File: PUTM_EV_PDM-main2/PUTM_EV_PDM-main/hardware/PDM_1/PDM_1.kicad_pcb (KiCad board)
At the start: 4 copper layers, 60 x 90 mm, 115 parts, among them IC2 BTS722204ESAXUMA1, IC3 BTS722204ESAXUMA1, IC4 BTS722204ESAXUMA1, IC5 BTS722204ESAXUMA1, U1 STM32G0C1KCTxN, U2 LD1117S33TR_SOT223, U3 LM2675M-5, U5 MCP2542FDxMF

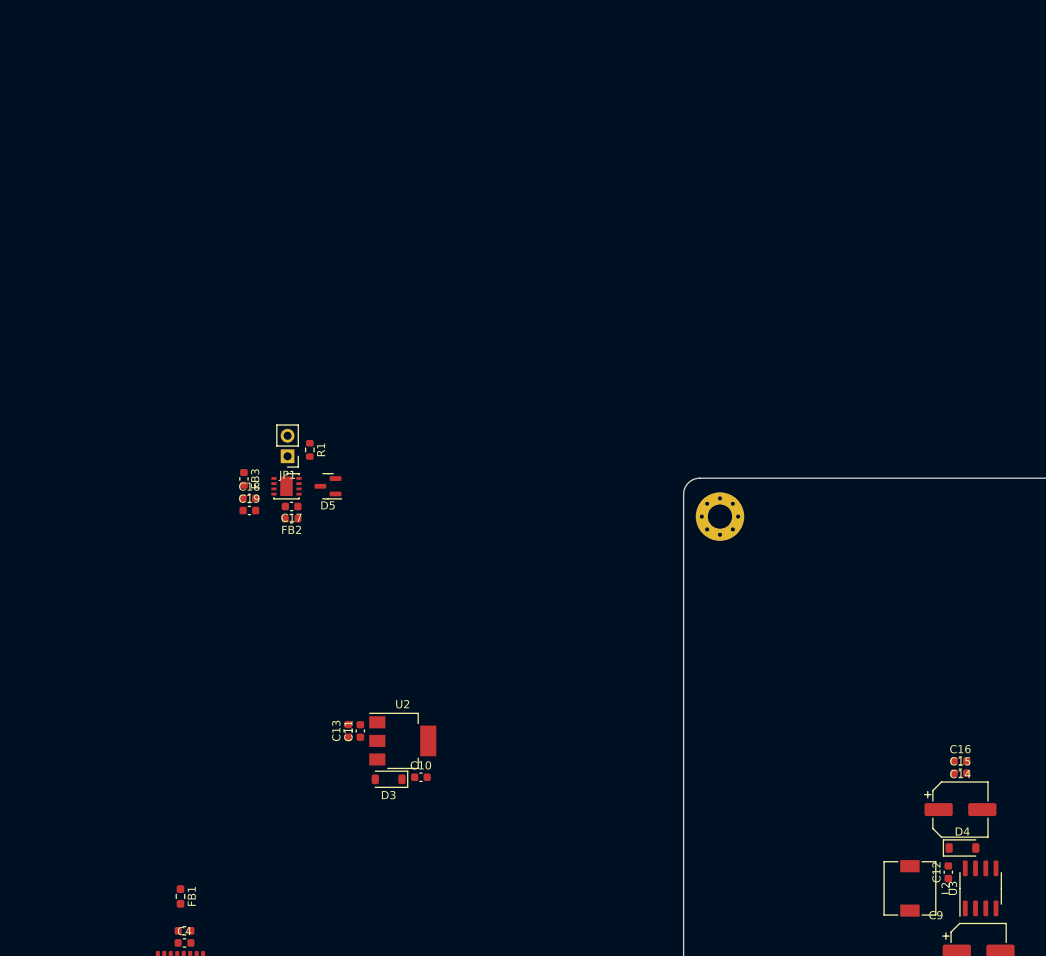
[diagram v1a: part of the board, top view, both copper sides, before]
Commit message: małe zmiany
dodano złącza
zmieniono parę footprintów
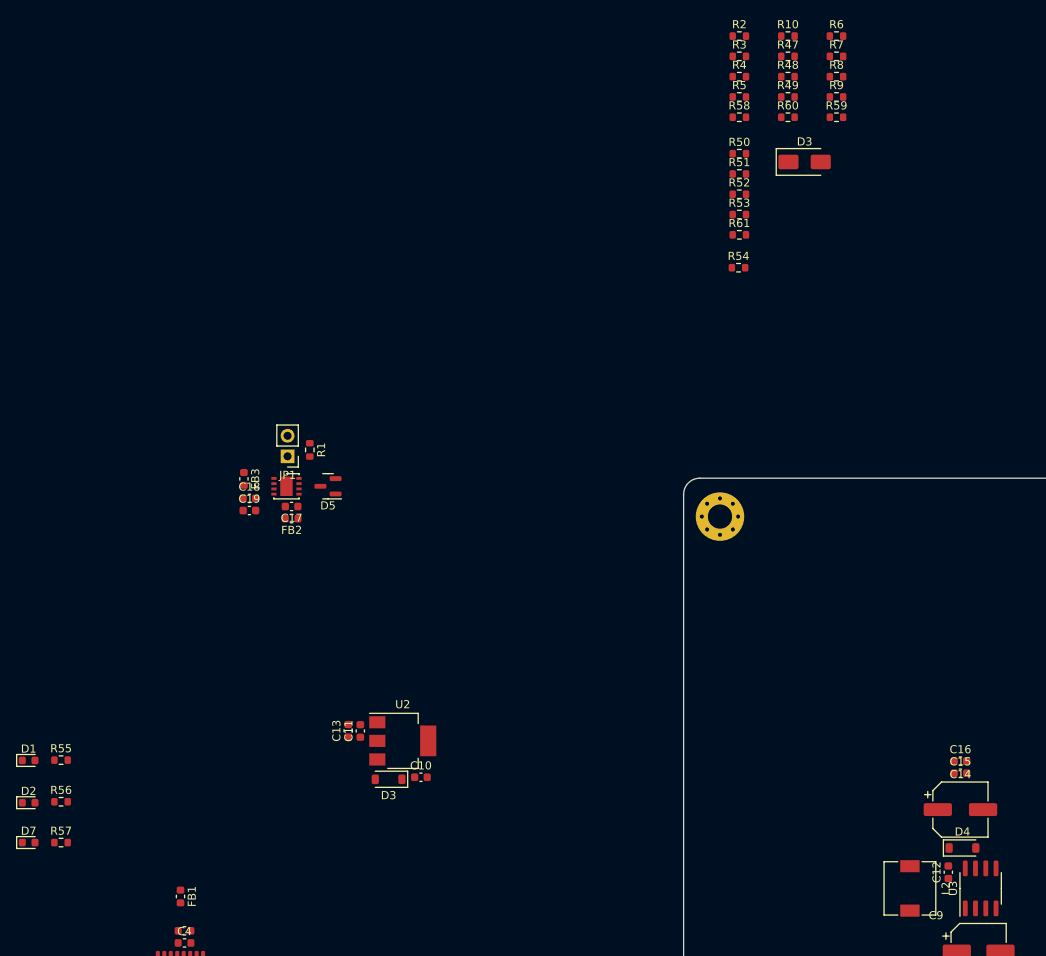
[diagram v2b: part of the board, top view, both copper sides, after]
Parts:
- added D1: LED, LED_SMD:LED_0603_1608Metric, F.Cu at (35.0, 110.9)
- added D2: LED, LED_SMD:LED_0603_1608Metric, F.Cu at (35.0, 116.2)
- added D3: PESD24VF1BLYL, Diode_SMD:D_SMA, F.Cu at (131.0, 36.9)
- added D7: LED, LED_SMD:LED_0603_1608Metric, F.Cu at (35.0, 121.1)
- added R10: 1.2k, Resistor_SMD:R_0603_1608Metric, F.Cu at (128.9, 21.3)
- added R2: 1.2k, Resistor_SMD:R_0603_1608Metric, F.Cu at (122.9, 21.3)
- added R3: 1.2k, Resistor_SMD:R_0603_1608Metric, F.Cu at (122.9, 23.8)
- added R4: 1.2k, Resistor_SMD:R_0603_1608Metric, F.Cu at (122.9, 26.3)
- added R47: 1.2k, Resistor_SMD:R_0603_1608Metric, F.Cu at (128.9, 23.8)
- added R48: 1.2k, Resistor_SMD:R_0603_1608Metric, F.Cu at (128.9, 26.3)
- added R49: 1.2k, Resistor_SMD:R_0603_1608Metric, F.Cu at (128.9, 28.8)
- added R5: 1.2k, Resistor_SMD:R_0603_1608Metric, F.Cu at (122.9, 28.8)
- added R50: 1.2k, Resistor_SMD:R_0603_1608Metric, F.Cu at (122.9, 35.9)
- added R51: 1.2k, Resistor_SMD:R_0603_1608Metric, F.Cu at (122.9, 38.4)
- added R52: 1.2k, Resistor_SMD:R_0603_1608Metric, F.Cu at (122.9, 40.9)
- added R53: 1.2k, Resistor_SMD:R_0603_1608Metric, F.Cu at (122.9, 43.4)
- added R54: 100k, Resistor_SMD:R_0603_1608Metric, F.Cu at (122.8, 50.0)
- added R55: 330, Resistor_SMD:R_0603_1608Metric, F.Cu at (39.0, 110.9)
- added R56: 330, Resistor_SMD:R_0603_1608Metric, F.Cu at (39.0, 116.0)
- added R57: 330, Resistor_SMD:R_0603_1608Metric, F.Cu at (39.0, 121.1)
- added R58: 4.7k, Resistor_SMD:R_0603_1608Metric, F.Cu at (122.9, 31.3)
- added R59: 4.7k, Resistor_SMD:R_0603_1608Metric, F.Cu at (134.9, 31.3)
- added R6: 1.2k, Resistor_SMD:R_0603_1608Metric, F.Cu at (134.9, 21.3)
- added R60: 4.7k, Resistor_SMD:R_0603_1608Metric, F.Cu at (128.9, 31.3)
- added R61: 4.7k, Resistor_SMD:R_0603_1608Metric, F.Cu at (122.9, 45.9)
- added R7: 1.2k, Resistor_SMD:R_0603_1608Metric, F.Cu at (134.9, 23.8)
- added R8: 1.2k, Resistor_SMD:R_0603_1608Metric, F.Cu at (134.9, 26.3)
- added R9: 1.2k, Resistor_SMD:R_0603_1608Metric, F.Cu at (134.9, 28.8)
- C14: footprint Capacitor_SMD:CP_Elec_6.3x7.7 -> Capacitor_SMD:CP_Elec_6.3x5.4
- FB1: footprint Resistor_SMD:R_0603_1608Metric_Pad0.98x0.95mm_HandSolder -> Inductor_SMD:L_0603_1608Metric
- R14, R15, R16, R17, R23, R24, R25, R26, R32, R33, R34, R35, R41, R42, R43, R44: value 4.7k -> 10k
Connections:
- net +24V renamed Net-(Dr1-A)
- net /battery connection/IC_1/out0 renamed OUT1_0
- net /battery connection/IC_1/out1 renamed OUT1_1
- net /battery connection/IC_1/out2 renamed OUT1_2
- net /battery connection/IC_1/out3 renamed OUT1_3
- net /battery connection/IC_2/out0 renamed OUT2_0
- net /battery connection/IC_2/out1 renamed OUT2_1
- net /battery connection/IC_2/out2 renamed OUT2_2
- net /battery connection/IC_2/out3 renamed OUT2_3
- net /battery connection/IC_3/out0 renamed OUT3_0
- net /battery connection/IC_3/out1 renamed OUT3_1
- net /battery connection/IC_3/out2 renamed OUT3_2
- net /battery connection/IC_3/out3 renamed OUT3_3
- net /battery connection/IC_4/out0 renamed OUT4_0
- net /battery connection/IC_4/out1 renamed OUT4_1
- net /battery connection/IC_4/out2 renamed OUT4_2
- net /battery connection/IC_4/out3 renamed OUT4_3
- C10 pad 1: Net-(D3-K) -> +5V
- C29 pad 1: /battery connection/IC_1/ADC -> /FUSE1_IS
- C30 pad 1: Net-(C30-Pad1) -> +BATT
- C31 pad 1: Net-(C30-Pad1) -> +BATT
- C31 pad 2: Net-(C31-Pad2) -> Net-(IC2-GND_1)
- C32 pad 1: Net-(C31-Pad2) -> Net-(IC2-GND_1)
- C37 pad 1: /battery connection/IC_2/ADC -> /FUSE2_IS
- C38 pad 1: Net-(C38-Pad1) -> +BATT
- C39 pad 1: Net-(C38-Pad1) -> +BATT
- C39 pad 2: Net-(C39-Pad2) -> Net-(IC3-GND_1)
- C40 pad 1: Net-(C39-Pad2) -> Net-(IC3-GND_1)
- C45 pad 1: /battery connection/IC_3/ADC -> /FUSE3_IS
- C46 pad 1: Net-(C46-Pad1) -> +BATT
- C47 pad 1: Net-(C46-Pad1) -> +BATT
- C47 pad 2: Net-(C47-Pad2) -> Net-(IC4-GND_1)
- C48 pad 1: Net-(C47-Pad2) -> Net-(IC4-GND_1)
- C53 pad 1: /battery connection/IC_4/ADC -> /FUSE4_IS
- C54 pad 1: Net-(C54-Pad1) -> +BATT
- C55 pad 1: Net-(C54-Pad1) -> +BATT
- C55 pad 2: Net-(C55-Pad2) -> Net-(IC5-GND_1)
- C56 pad 1: Net-(C55-Pad2) -> Net-(IC5-GND_1)
- IC2 pad 1: unconnected-(IC2-GND_1-Pad1) -> Net-(IC2-GND_1)
- IC2 pad 11: /battery connection/IC_1/4.7k resistor -> /battery connection/IC_1/IN3
- IC2 pad 3: /battery connection/IC_1/1.2k resistor -> Net-(IC2-SO)
- IC2 pad 4: /battery connection/IC_1/1.2k resistor -> Net-(IC2-SI)
- IC2 pad 5: /battery connection/IC_1/1.2k resistor -> Net-(IC2-SCLK)
- IC2 pad 6: /battery connection/IC_1/1.2k resistor -> Net-(IC2-CSN)
- IC2 pad 7: unconnected-(IC2-LHI-Pad7) -> Net-(IC2-LHI)
- IC3 pad 1: unconnected-(IC3-GND_1-Pad1) -> Net-(IC3-GND_1)
- IC3 pad 11: /battery connection/IC_2/4.7k resistor -> /battery connection/IC_2/IN3
- IC3 pad 3: /battery connection/IC_1/1.2k resistor -> Net-(IC3-SO)
- IC3 pad 4: /battery connection/IC_1/1.2k resistor -> Net-(IC3-SI)
- IC3 pad 5: /battery connection/IC_1/1.2k resistor -> Net-(IC3-SCLK)
- IC3 pad 6: /battery connection/IC_1/1.2k resistor -> Net-(IC3-CSN)
- IC3 pad 7: unconnected-(IC3-LHI-Pad7) -> Net-(IC3-LHI)
- IC4 pad 1: unconnected-(IC4-GND_1-Pad1) -> Net-(IC4-GND_1)
- IC4 pad 11: /battery connection/IC_3/4.7k resistor -> /battery connection/IC_3/IN3
- IC4 pad 3: /battery connection/IC_1/1.2k resistor -> Net-(IC4-SO)
- IC4 pad 4: /battery connection/IC_1/1.2k resistor -> Net-(IC4-SI)
- IC4 pad 5: /battery connection/IC_1/1.2k resistor -> Net-(IC4-SCLK)
- IC4 pad 6: /battery connection/IC_1/1.2k resistor -> Net-(IC4-CSN)
- IC4 pad 7: unconnected-(IC4-LHI-Pad7) -> Net-(IC4-LHI)
- IC5 pad 1: unconnected-(IC5-GND_1-Pad1) -> Net-(IC5-GND_1)
- IC5 pad 11: /battery connection/IC_4/4.7k resistor -> /battery connection/IC_4/IN3
- IC5 pad 3: /battery connection/IC_1/1.2k resistor -> Net-(IC5-SO)
- IC5 pad 4: /battery connection/IC_1/1.2k resistor -> Net-(IC5-SI)
- IC5 pad 5: /battery connection/IC_1/1.2k resistor -> Net-(IC5-SCLK)
- IC5 pad 6: /battery connection/IC_1/1.2k resistor -> Net-(IC5-CSN)
- IC5 pad 7: unconnected-(IC5-LHI-Pad7) -> Net-(IC5-LHI)
- R11 pad 1: /battery connection/IC_1/ADC -> /FUSE1_IS
- R14 pad 1: /battery connection/IC_1/IN0 -> GND
- R15 pad 1: /battery connection/IC_1/IN1 -> GND
- R16 pad 1: /battery connection/IC_1/IN2 -> GND
- R17 pad 1: /battery connection/IC_1/IN3 -> GND
- R17 pad 2: /battery connection/IC_1/4.7k resistor -> /battery connection/IC_1/IN3
- R18 pad 2: Net-(C31-Pad2) -> Net-(IC2-GND_1)
- R20 pad 1: /battery connection/IC_2/ADC -> /FUSE2_IS
- R23 pad 1: /battery connection/IC_2/IN0 -> GND
- R24 pad 1: /battery connection/IC_2/IN1 -> GND
- R25 pad 1: /battery connection/IC_2/IN2 -> GND
- R26 pad 1: /battery connection/IC_2/IN3 -> GND
- R26 pad 2: /battery connection/IC_2/4.7k resistor -> /battery connection/IC_2/IN3
- R27 pad 2: Net-(C39-Pad2) -> Net-(IC3-GND_1)
- R29 pad 1: /battery connection/IC_3/ADC -> /FUSE3_IS
- R32 pad 1: /battery connection/IC_3/IN0 -> GND
- R33 pad 1: /battery connection/IC_3/IN1 -> GND
- R34 pad 1: /battery connection/IC_3/IN2 -> GND
- R35 pad 1: /battery connection/IC_3/IN3 -> GND
- R35 pad 2: /battery connection/IC_3/4.7k resistor -> /battery connection/IC_3/IN3
- R36 pad 2: Net-(C47-Pad2) -> Net-(IC4-GND_1)
- R38 pad 1: /battery connection/IC_4/ADC -> /FUSE4_IS
- R41 pad 1: /battery connection/IC_4/IN0 -> GND
- R42 pad 1: /battery connection/IC_4/IN1 -> GND
- R43 pad 1: /battery connection/IC_4/IN2 -> GND
- R44 pad 1: /battery connection/IC_4/IN3 -> GND
- R44 pad 2: /battery connection/IC_4/4.7k resistor -> /battery connection/IC_4/IN3
- R45 pad 2: Net-(C55-Pad2) -> Net-(IC5-GND_1)
- U1 pad 10: unconnected-(U1-PA3-Pad10) -> /FUSE4_IS
- U1 pad 11: unconnected-(U1-PA4-Pad11) -> /SPI1_NSS
- U1 pad 12: unconnected-(U1-PA5-Pad12) -> /SPI1_SCK
- U1 pad 13: unconnected-(U1-PA6-Pad13) -> /SPI1_MISO
- U1 pad 14: unconnected-(U1-PA7-Pad14) -> /SPI1_MOSI
- U1 pad 15: unconnected-(U1-PB0-Pad15) -> /LHI
- U1 pad 17: unconnected-(U1-PB15-Pad17) -> /LED3
- U1 pad 18: unconnected-(U1-PA8-Pad18) -> /LED1
- U1 pad 19: unconnected-(U1-PA9/UCPD1_DBCC1-Pad19) -> /LED2
- U1 pad 22: unconnected-(U1-PA11/PA9-Pad22) -> /CAN_RXD
- U1 pad 23: unconnected-(U1-PA12/PA10-Pad23) -> /CAN_TXD
- U1 pad 24: unconnected-(U1-PA13-Pad24) -> /SWDIO
- U1 pad 25: unconnected-(U1-PA14-Pad25) -> /SWCLK
- U1 pad 30: unconnected-(U1-PB6-Pad30) -> /USART1_TX
- U1 pad 31: unconnected-(U1-PB7-Pad31) -> /USART1_RX
- U1 pad 6: unconnected-(U1-PF2-Pad6) -> /NRST
- U1 pad 7: unconnected-(U1-PA0-Pad7) -> /FUSE1_IS
- U1 pad 8: unconnected-(U1-PA1-Pad8) -> /FUSE2_IS
- U1 pad 9: unconnected-(U1-PA2-Pad9) -> /FUSE3_IS
- U2 pad 3: Net-(D3-K) -> +5V

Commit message: piny na płytce
Dodano ułożenie pinów na płytce
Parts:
- added F1: 2920L050_72DR, 2920l:FUSC7451X125N, F.Cu at (158.8, 151.6)
- added J1: FTSH-107-01-L-DV-K-A, FTSH-107-01-L-DV-K-A:FTSH-107-XX-YYY-DV-K-A, F.Cu at (84.9, 171.9)
- added J2: UPT-08-01-01-L-RA, proper_8pin:UPT080101LRA, F.Cu at (178.5, 94.7)
- added J5: UPT-02-01-01-X-RA, 2pin:SAMTEC_UPT-02-01-01-X-RA, F.Cu at (177.0, 151.1)
- added J6: Conn_01x06, Connector_IDC:IDC-Header_2x03_P2.54mm_Vertical, F.Cu at (85.7, 33.7)
- added J7: UPT-08-01-01-L-RA, proper_8pin:UPT080101LRA, F.Cu at (178.5, 135.8)
- moved R10 125.1 mm to (206.6, 119.4)
- moved R47 125.1 mm to (206.6, 121.9)
- moved R48 125.1 mm to (206.6, 124.4)
- moved R49 125.1 mm to (206.6, 126.9)
- moved R60 125.1 mm to (206.6, 129.4)
- moved R54 120.9 mm to (87.4, 165.5), turned to -90 degrees
- moved D3 110.1 mm to (156.3, 144.0), turned to -90 degrees
- moved R52 98.9 mm to (205.6, 95.2)
- moved R50 98.9 mm to (205.6, 90.1)
- moved R51 98.9 mm to (205.6, 92.7)
- moved R53 98.9 mm to (205.6, 97.7)
- moved R61 98.9 mm to (205.6, 100.2)
- moved R2 84.4 mm to (205.5, 38.5)
- moved R3 84.4 mm to (205.5, 41.0)
- moved R4 84.4 mm to (205.5, 43.5)
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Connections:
- net /CAN_H renamed CAN_H
- net /CAN_L renamed CAN_L
- R58 pad 1: /LHI -> /LHI_1
- R59 pad 1: /LHI -> /LHI_2
- R60 pad 1: /LHI -> /LHI_3
- R61 pad 1: /LHI -> /LHI_4
- U1 pad 15: /LHI -> /LHI_3
- U1 pad 16: unconnected-(U1-PB1-Pad16) -> /LHI_4
- U1 pad 28: unconnected-(U1-PD2-Pad28) -> /LHI_1
- U1 pad 29: unconnected-(U1-PD3-Pad29) -> /LHI_2
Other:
- board size 60 x 90 mm -> 80 x 100 mm

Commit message: Zamienione 2 i 8 pin
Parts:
- moved J5 82.1 mm to (177.0, 68.9)
- moved J2 18.2 mm to (178.5, 112.9)
- moved J7 18.2 mm to (178.5, 154.0)
- moved REF** 16.7 mm to (104.0, 64.0)
- moved REF** 3.20 mm to (164.0, 64.0)
- moved REF** 2.75 mm to (104.0, 156.0)
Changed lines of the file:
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@@
   )
   (footprint "proper_8pin:UPT080101LRA" (layer "F.Cu")
-    (at 178.5 135.77 90)
+    (at 178.5 153.965 90)
     (descr "UPT-08-01-01-L-RA-2")
     (tags "Connector")
@@
   )
   (footprint "MountingHole:MountingHole_3mm_Pad_Via" (layer "F.Cu")
-    (at 161.5 66)
+    (at 164 64)
     (descr "Mounting Hole 3mm")
     (tags "mounting hole 3mm")
@@
   )
   (footprint "2pin:SAMTEC_UPT-02-01-01-X-RA" (layer "F.Cu")
-    (at 177 151.06 90)
+    (at 177 68.94 90)
     (property "MANUFACTURER" "Samtec")
     (property "MAXIMUM_PACKAGE_HEIGHT" "9.0mm")
@@
   )
   (footprint "MountingHole:MountingHole_3mm_Pad_Via" (layer "F.Cu")
-    (at 106.59099 155.09099)
+    (at 104 156)
     (descr "Mounting Hole 3mm")
     (tags "mounting hole 3mm")
@@
   )
   (footprint "MountingHole:MountingHole_3mm_Pad_Via" (layer "F.Cu")
-    (at 120.5 66.31)
+    (at 104 64)
     (descr "Mounting Hole 3mm")
     (tags "mounting hole 3mm")
@@
   )
   (footprint "proper_8pin:UPT080101LRA" (layer "F.Cu")
-    (at 178.5 94.705 90)
+    (at 178.5 112.905 90)
     (descr "UPT-08-01-01-L-RA-2")
     (tags "Connector")

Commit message: Połączenia w grupach
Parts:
- removed D12: PESD24VF1BLYL, Diode_SMD:D_SMA
- removed L2: 47u, Inductor_SMD:L_6.3x6.3_H3
- added L4: 47u, Inductor_SMD:L_6.3x6.3_H3, F.Cu at (135.0, 66.6)
- C49, C50, C51, C52: moved to B.Cu
- Dr1: value 1N5822 -> SS34ALH
- U3: value LM2675M-5 -> LM2675M-5.0/NOPB
- moved D8 97.8 mm to (151.9, 115.4), turned to 180 degrees
- moved R11 95.3 mm to (153.6, 117.9), turned to 180 degrees
- moved R13 92.0 mm to (157.0, 114.4), turned to 0 degrees
- moved C31 90.7 mm to (155.2, 102.8)
- moved C30 90.7 mm to (151.8, 102.8)
- moved C32 90.7 mm to (156.1, 105.1)
- moved IC2 90.7 mm to (160.6, 109.0)
- moved R12 90.7 mm to (153.6, 105.8)
- moved R18 90.7 mm to (153.6, 104.2)
- moved R14 90.6 mm to (155.2, 108.3)
- moved R15 90.6 mm to (155.2, 109.8)
- moved R16 90.6 mm to (155.2, 111.3)
- moved R17 90.6 mm to (155.2, 112.8)
- moved C35 90.4 mm to (166.1, 109.9)
- moved C33 90.4 mm to (166.1, 106.9)
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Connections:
- net Net-(Dr1-A) renamed /power/VIN
- net Net-(U1-VDD) renamed /STM_VCC
- net Net-(U3-CB) renamed /power/CB
- D3 pad 1: Net-(D3-K) -> GND
- D3 pad 2: +5V -> /power/VIN_L
- F1 pad 2: +24V -> +BATT
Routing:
- net +5V: track 0.00 -> 13.3 mm
- net Net-(IC4-LHI): track 0.00 -> 10.5 mm
- net Net-(IC4-SO): track 0.00 -> 10.3 mm
- net Net-(IC4-CSN): track 0.00 -> 10.2 mm
- net Net-(IC4-SI): track 0.00 -> 9.92 mm
- net Net-(IC4-SCLK): track 0.00 -> 9.81 mm
- net /battery connection/IC_3/IN0: track 0.00 -> 8.32 mm
- net GND: track 0.00 -> 7.45 mm, vias 0 -> 7
- net Net-(U5-VDD): track 0.00 -> 7.07 mm
- net /STM_VCC: track 0.00 -> 6.83 mm
- net Net-(IC4-GND_1): track 0.00 -> 6.65 mm
- net /battery connection/IC_3/IN1: track 0.00 -> 6.55 mm
- net Net-(JP1-B): track 0.00 -> 4.82 mm
- net /battery connection/IC_3/IN2: track 0.00 -> 4.78 mm
- net Net-(D10-K): track 0.00 -> 4.70 mm
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- added copper zone on F.Cu, net +5V
- added copper zone on F.Cu, net /power/CB
- added copper zone on F.Cu, net /power/SW_L
- added copper zone on F.Cu, net /power/VIN
- added copper zone on F.Cu, net /power/VIN_L
- added copper zone on F.Cu, net /power/VIN_SW_REG

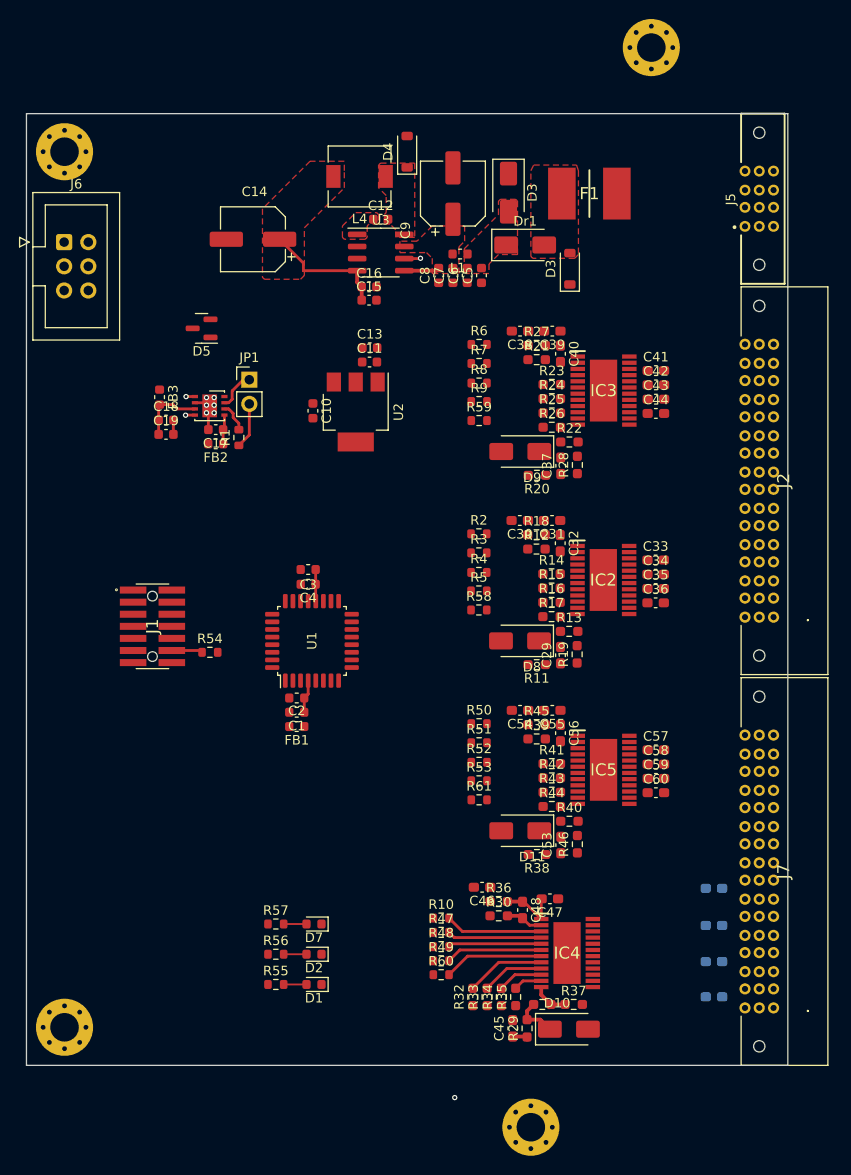
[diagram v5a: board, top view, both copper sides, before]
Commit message: Nowe ułożenie na płytce
Ułożenie komponentów na płytce
Dodane połączenie +24V
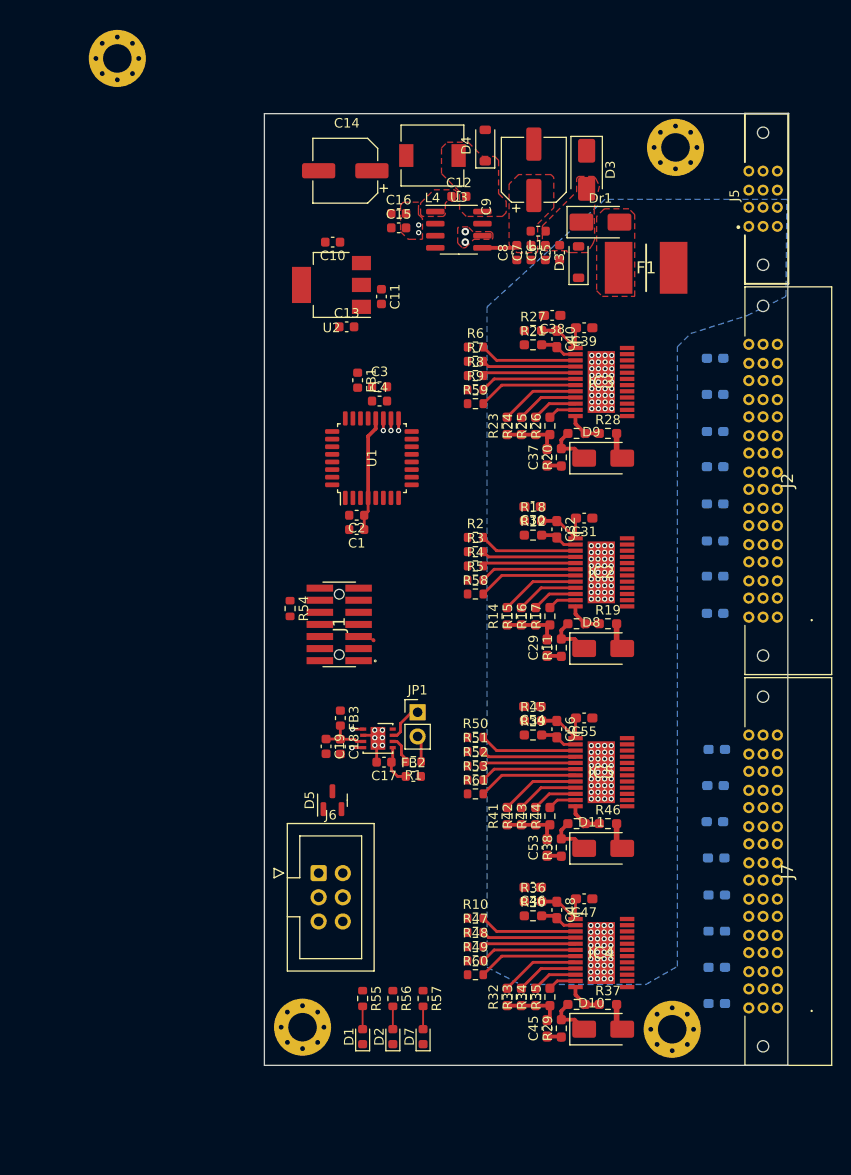
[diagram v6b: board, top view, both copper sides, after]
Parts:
- C33, C34, C35, C36, C41, C42, C43, C44, C57, C58, C59, C60: moved to B.Cu
- moved J6 71.5 mm to (130.7, 139.8)
- moved D5 51.4 mm to (132.2, 132.1), turned to 90 degrees
- moved FB2 40.6 mm to (140.7, 129.6), turned to 0 degrees
- moved C17 39.2 mm to (137.6, 128.1)
- moved JP1 39.2 mm to (141.1, 122.9)
- moved U5 39.2 mm to (136.9, 125.6)
- moved C18 38.9 mm to (133.0, 126.5), turned to -90 degrees
- moved FB3 38.7 mm to (133.0, 123.5)
- moved R1 38.7 mm to (140.7, 128.1), turned to 180 degrees
- moved FB1 36.9 mm to (134.8, 88.0), turned to -90 degrees
- moved C19 36.8 mm to (131.5, 126.5), turned to -90 degrees
- moved REF** 25.0 mm to (129.0, 156.0)
- moved C4 20.7 mm to (137.1, 90.2), turned to 0 degrees
- moved C3 20.6 mm to (137.1, 88.7), turned to 0 degrees
- moved U1 20.2 mm to (136.3, 96.2)
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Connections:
- net Net-(U5-VDD) renamed /CAN/CAN_VDD
- J5 pad P01_1: +BATT -> (no net)
- J5 pad P02_1: GND -> (no net)
- U1 pad 18: /LED1 -> /LED2
- U1 pad 19: /LED2 -> /LED1
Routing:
- net GND: track 7.45 -> 40.3 mm, vias 7 -> 10
- net +5V: track 13.3 -> 0.00 mm
- net Net-(IC5-LHI): track 0.00 -> 10.5 mm
- net Net-(IC3-LHI): track 0.00 -> 10.5 mm
- net Net-(IC2-LHI): track 0.00 -> 10.5 mm
- net Net-(IC5-SO): track 0.00 -> 10.3 mm
- net Net-(IC3-SO): track 0.00 -> 10.3 mm
- net Net-(IC2-SO): track 0.00 -> 10.3 mm
- net Net-(IC3-CSN): track 0.00 -> 10.2 mm
- net Net-(IC2-CSN): track 0.00 -> 10.2 mm
- net Net-(IC5-CSN): track 0.00 -> 10.2 mm
- net Net-(IC5-SI): track 0.00 -> 9.92 mm
- net Net-(IC3-SI): track 0.00 -> 9.92 mm
- net Net-(IC2-SI): track 0.00 -> 9.92 mm
- net Net-(IC5-SCLK): track 0.00 -> 9.81 mm
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- added copper zone on B.Cu, net +BATT
- added copper zone on F.Cu, net GND
- removed copper zone on F.Cu, net +5V
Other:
- board size 80 x 100 mm -> 55 x 100 mm
